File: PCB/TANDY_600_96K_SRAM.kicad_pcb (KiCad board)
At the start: 2 copper layers, 68.6 x 45.1 mm, 7 parts, among them J1 DIN-41612-44-M-RA, U1 628128_DIP32_SSOP32, U2 74HC148

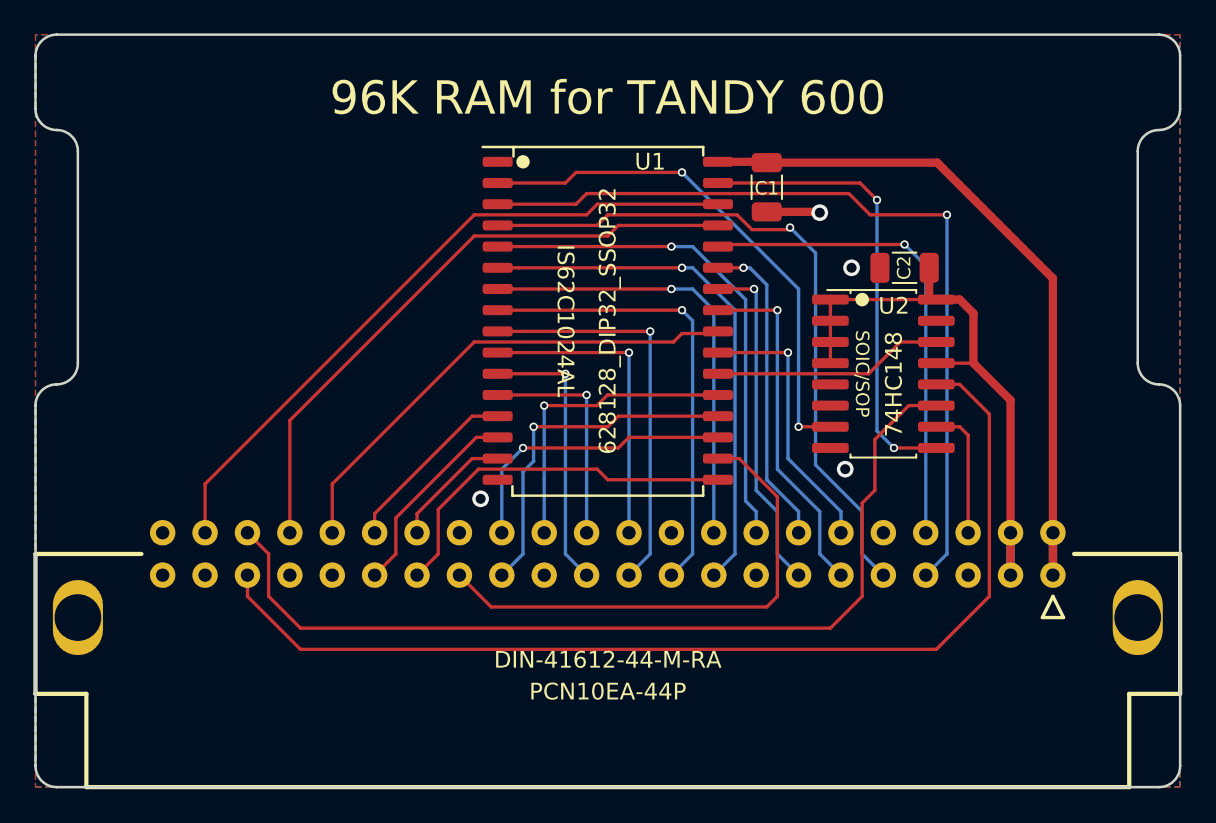
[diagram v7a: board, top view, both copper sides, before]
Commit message: silkscreen, readme, pics
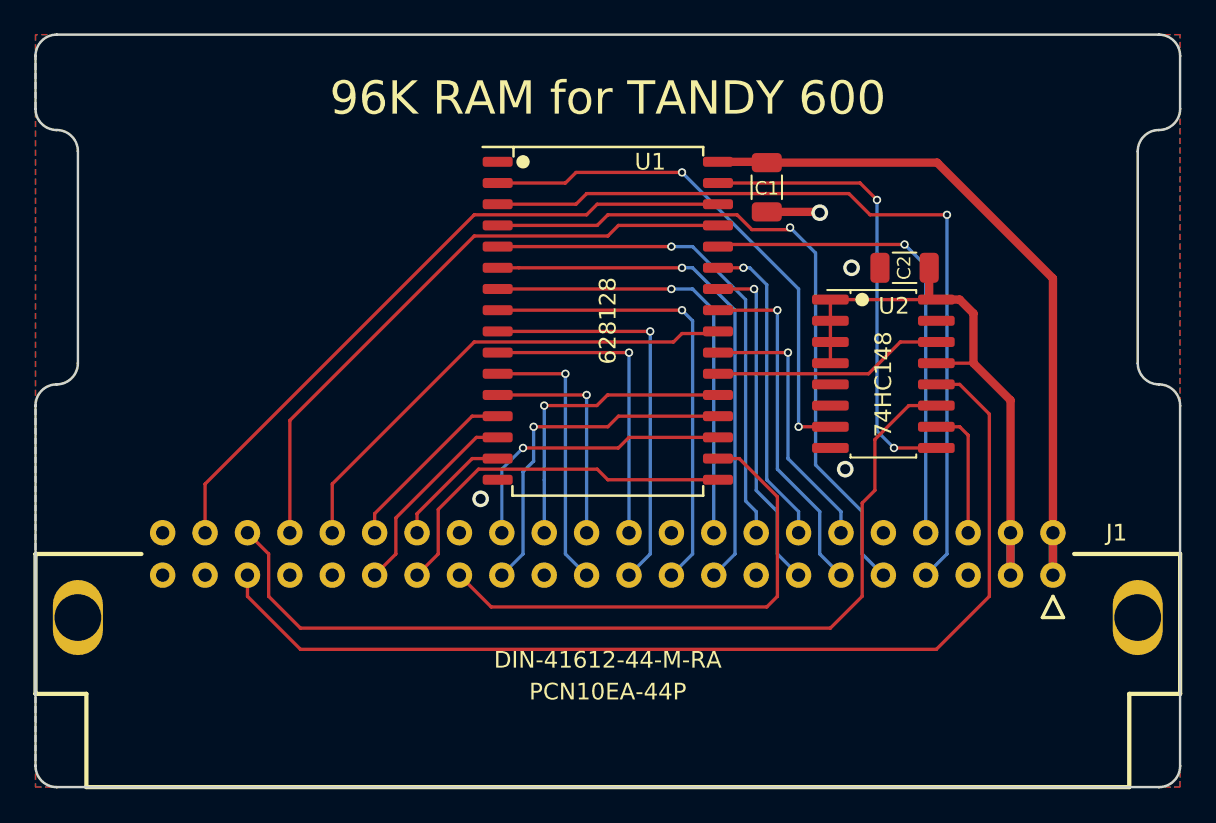
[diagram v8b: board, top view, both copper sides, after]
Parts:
- U1: value 628128_DIP32_SSOP32 -> 628128
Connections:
- J1 pad 15B: (no net) -> unconnected-(J1-Pad15B)
- J1 pad 21A: (no net) -> unconnected-(J1-Pad21A)
- U1 pad 1: (no net) -> unconnected-(U1-Pad1)
- U2 pad 15: (no net) -> unconnected-(U2-Pad15)
- U2 pad 6: (no net) -> unconnected-(U2-Pad6)
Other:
- board text removed: "IS62C1024AL"
- board text removed: "SOIC/SOP"
